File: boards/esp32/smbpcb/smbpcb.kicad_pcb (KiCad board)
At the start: 2 copper layers, 85.4 x 70.4 mm, 66 parts, among them IC1 MiCS-6814, J1 USB_B_Micro, J2 PMS7003, Q1 SUD08P06-155L, SW1 RESET, SW2 RESET, U1 MCP73831-2-OT, U2 SGM6603-5.0YN6G_TR, U3 ESP32-WROOM-32, U4 SSD1306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

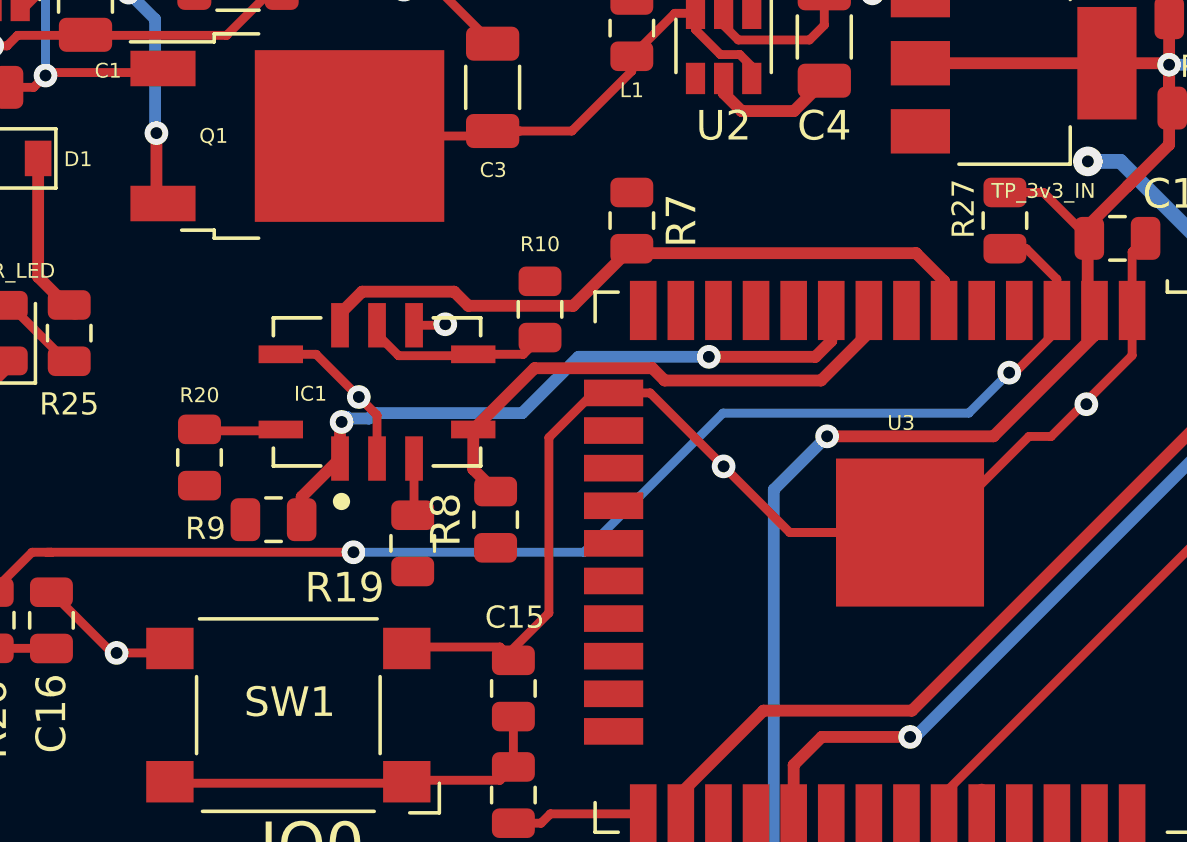
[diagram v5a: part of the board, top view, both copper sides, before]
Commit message: fixed mics pullups
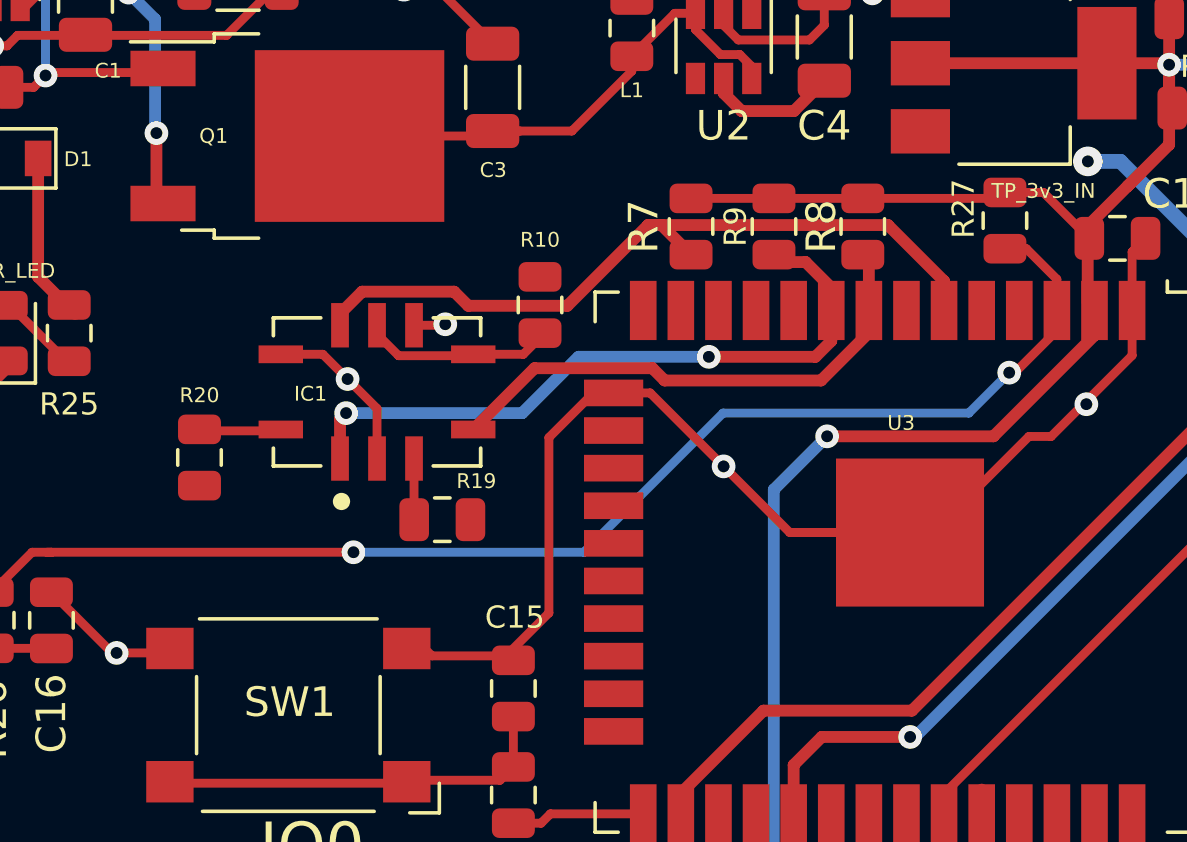
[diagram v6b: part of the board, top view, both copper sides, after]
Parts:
- moved R9 19.6 mm to (70.2, 53.8), turned to -90 degrees
- moved R8 15.9 mm to (73.2, 53.8), turned to -90 degrees
- moved R7 2.01 mm to (67.4, 53.8)
- moved R19 1.28 mm to (59.0, 63.7), turned to 0 degrees
- moved R10 0.15 mm to (62.3, 56.5)
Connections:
- R7 pad 1: +5V -> +3V3
- R8 pad 1: +5V -> +3V3
- R9 pad 1: +5V -> +3V3
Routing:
- net +3V3: track 215.3 -> 226.0 mm
- net CO: track 23.4 -> 26.1 mm
- net NO2: track 22.6 -> 23.1 mm
